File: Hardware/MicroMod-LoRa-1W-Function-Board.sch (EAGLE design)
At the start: 34 parts, among them J11 MICROMOD_STANDARD, Q3 20V/4.2A/52mΩ/1.4W, Q4 600mA/40V, Q5 20V/4.2A/52mΩ/1.4W, Q6 600mA/40V, U1 EEPROM, U4 E19-915M30S

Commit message: Adding panel files
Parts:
- added LOGO2: SPECIAL_INSTRUCTIONS-ORDERING, SparkFun-Aesthetics:SPECIAL_INSTRUCTIONS-ORDERING
- C8: value 68uF -> 47uF; device SparkFun-Capacitors:68UF-POLAR-EIA3528-10V-10%(TANT) -> SparkFun-Capacitors:47UF-POLAR-EIA3528-10V-10%
- J11: device SparkFun-MicroMod-Test:MICROMOD_STANDARD -> SparkFun-MicroMod-Function:MICROMOD_STANDARD
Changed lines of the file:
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@@
 <part name="GND33" library="SparkFun-PowerSymbols" deviceset="GND" device=""/>
 <part name="GND34" library="SparkFun-PowerSymbols" deviceset="GND" device=""/>
-<part name="C8" library="SparkFun-Capacitors" deviceset="68UF-POLAR" device="-EIA3528-10V-10%(TANT)" value="68uF"/>
+<part name="C8" library="SparkFun-Capacitors" deviceset="47UF-POLAR" device="-EIA3528-10V-10%" value="47uF"/>
 <part name="GND2" library="SparkFun-PowerSymbols" deviceset="GND" device=""/>
 <part name="SUPPLY2" library="SparkFun-PowerSymbols" deviceset="VCC" device=""/>
@@
 <part name="E1" library="SparkFun-RF" deviceset="ANTENNA-SMA-GROUNDED" device="EDGE_RPSMA_SMD" value="RP-SMA"/>
 <part name="GND3" library="SparkFun-PowerSymbols" deviceset="GND" device=""/>
-<part name="J11" library="SparkFun-MicroMod-Test" deviceset="MICROMOD" device="_STANDARD"/>
+<part name="J11" library="SparkFun-MicroMod-Function" deviceset="MICROMOD" device="_STANDARD"/>
 <part name="R2" library="SparkFun-Resistors" deviceset="470OHM" device="-0603-1/10W-1%" value="470"/>
 <part name="Q3" library="SparkFun-DiscreteSemi" deviceset="MOSFET_PCH" device="-DMG2305UX-7" value="20V/4.2A/52mΩ/1.4W"/>
@@
 <part name="C4" library="SparkFun-Capacitors" deviceset="0.1UF" device="-0603-25V-(+80/-20%)" value="0.1uF"/>
 <part name="GND10" library="SparkFun-PowerSymbols" deviceset="GND" device=""/>
+<part name="LOGO2" library="SparkFun-Aesthetics" deviceset="SPECIAL_INSTRUCTIONS" device="-ORDERING"/>
 </parts>
 <sheets>
@@
 <attribute name="VALUE" x="5.08" y="17.526" size="1.778" layer="96" align="top-center"/>
 </instance>
+<instance part="LOGO2" gate="G$1" x="226.06" y="22.86" smashed="yes"/>
 </instances>
 <busses>

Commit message: Fix power control circuit. Add example sketch. Add x02 production panels.
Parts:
- removed Q3, Q5: 20V/4.2A/52mΩ/1.4W, SparkFun-DiscreteSemi:MOSFET_PCH-DMG2305UX-7
- removed Q4: 600mA/40V, SparkFun-DiscreteSemi:TRANS_PNP-MMBT4403
- removed R7: 100k, SparkFun-Resistors:100KOHM-0603-1/10W-1%
- added JP1: JUMPER-SMT_2_NO_SILK, SparkFun-Jumpers:JUMPER-SMT_2_NO_SILK
- added Q2: 20V/4.2A/52mΩ/1.4W, SparkFun-DiscreteSemi:MOSFET_PCH-DMG2305UX-7
- added Q8, Q9: 5.8A/30V/35mΩ, SparkFun-DiscreteSemi:MOSFET-NCH-AO3404A
- added R1, R3: 10k, SparkFun-Resistors:10KOHM-0603-1/10W-1%
- Q6: value 600mA/40V -> 20V/4.2A/52mΩ/1.4W; device SparkFun-DiscreteSemi:TRANS_PNP-MMBT4403 -> SparkFun-DiscreteSemi:MOSFET_PCH-DMG2305UX-7
- R4: value 100k -> 10k; device SparkFun-Resistors:100KOHM-0603-1/10W-1% -> SparkFun-Resistors:10KOHM-0603-1/10W-1%
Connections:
- removed net N$11: Q5.G, Q6.C, R7.2
- removed net N$9: Q3.G, Q4.C, R4.2
- new net N$2: Q2.G, Q8.D, R1.1
- new net N$3: Q6.G, Q9.D, R3.1
- new net N$7: JP1.2, R4.1, U1.WP
- net 3.3V: now also Q2.D, R4.2; no longer Q3.D
- net 3.3V_IN: now also Q2.S, R1.2; no longer Q3.S, Q4.E
- net GND: now also JP1.1, Q8.S, Q9.S; no longer R4.1, R7.1, U1.WP
- net PWR_EN: now also Q8.G, Q9.G; no longer Q4.B, Q6.B
- net VCC: now also Q6.D; no longer Q5.D
- net VCC_IN: now also Q6.S, R3.2; no longer Q5.S, Q6.E
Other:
- note added: "VCC: 3.3-5.5V >= 5V Ensures Max Output Power"
- note removed: "0V turns on PNP"
- note removed: "3.3V on gate turns off MOSFET"
- note removed: "VCC: 3.3-5.5V >= 5V Ensures Output Power"
- moved on the sheet: R4

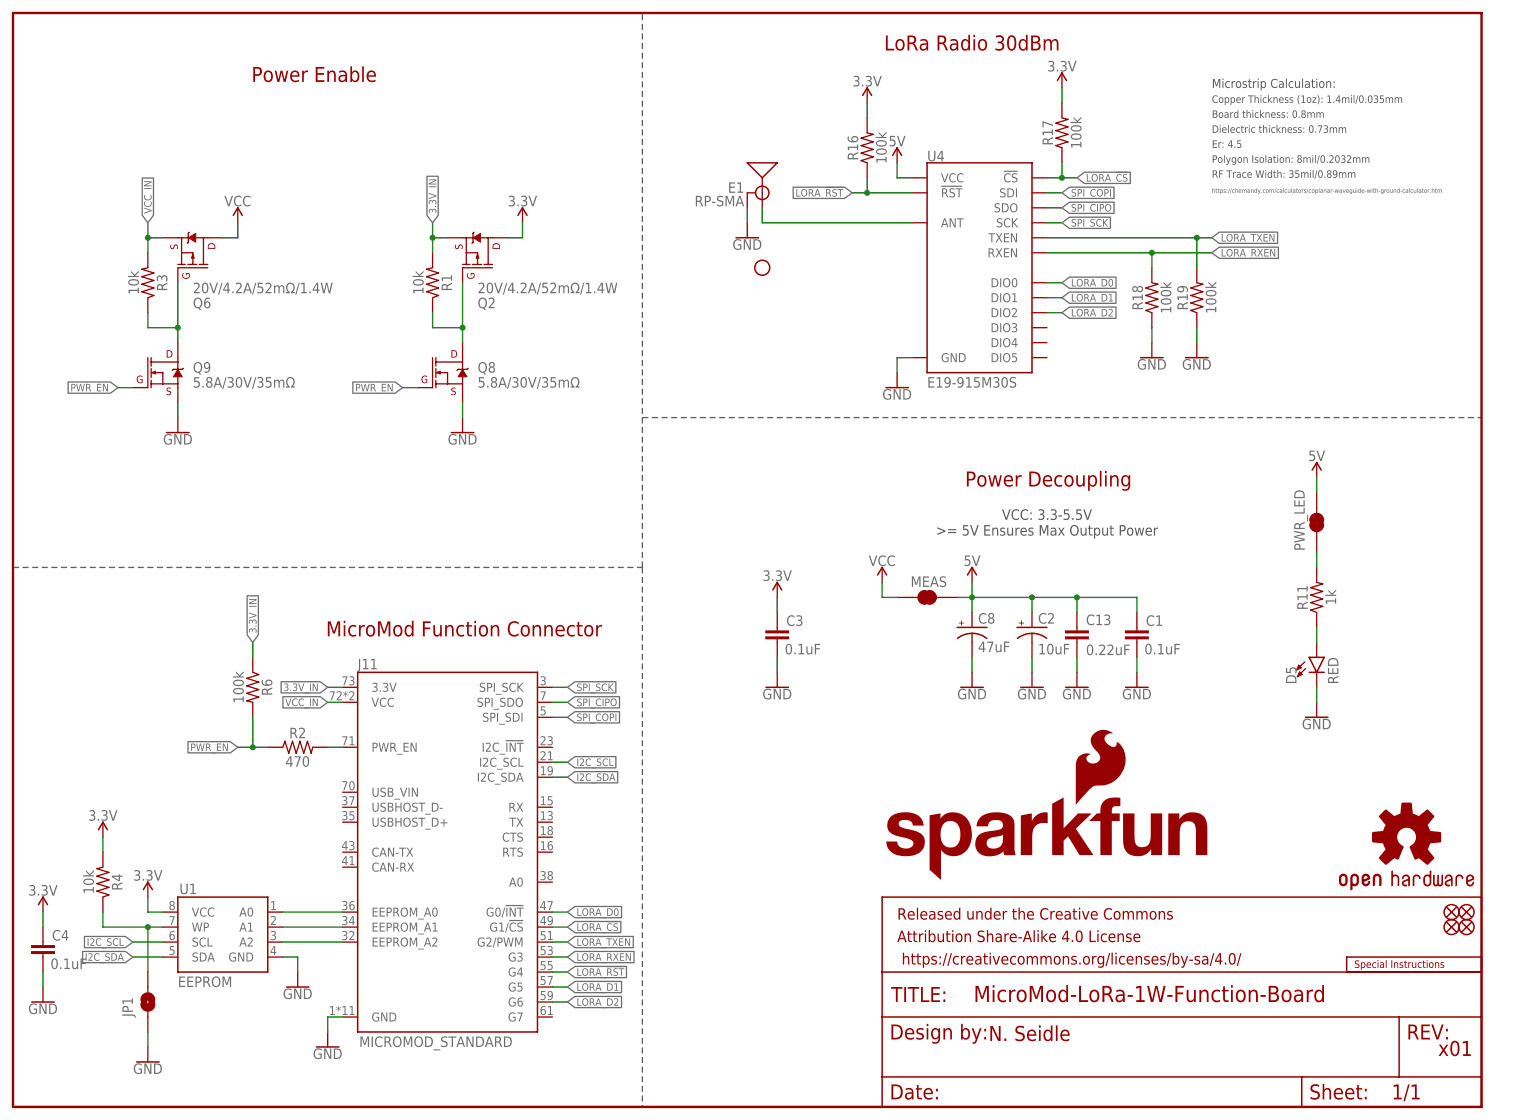
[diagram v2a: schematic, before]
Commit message: Add WP access to card edge.
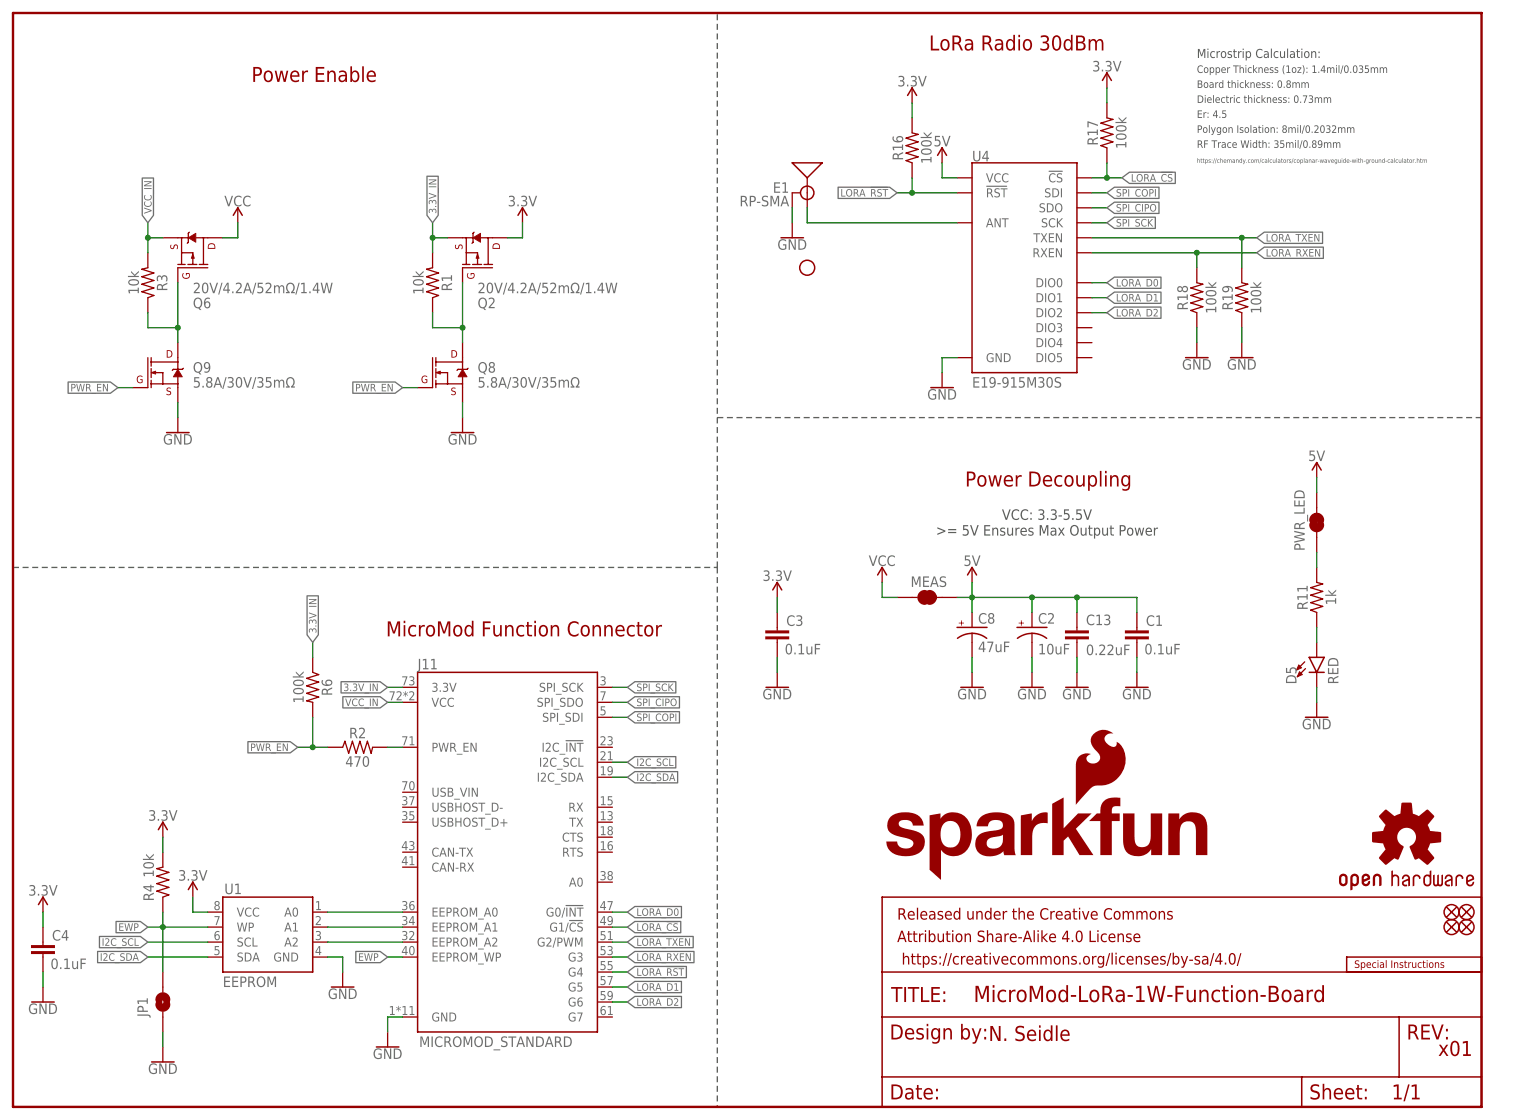
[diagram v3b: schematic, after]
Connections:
- removed net N$7: JP1.2, R4.1, U1.WP
- new net EWP: J11.EEPROM_WP, JP1.2, R4.1, U1.WP
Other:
- moved on the sheet: E1, JP1, R16, R17, R18, R19, R2, R4, R6, U1, U4

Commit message: Update version to v10.
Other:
- note added: "v10"
- note removed: "x01"
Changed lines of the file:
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@@
 &gt;= 5V Ensures Max Output Power</text>
 <text x="165.354" y="11.176" size="2.54" layer="94">N. Seidle</text>
-<text x="241.554" y="8.636" size="2.54" layer="94">x01</text>
+<text x="241.554" y="8.636" size="2.54" layer="94">v10</text>
 <text x="170.18" y="180.34" size="2.54" layer="94" font="vector" align="center">LoRa Radio 30dBm</text>
 <text x="200.66" y="172.72" size="1.27" layer="97">Board thickness: 0.8mm</text>

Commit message: Add SMA center pin. Increase panel gap to facilitate center pin. PCB is still v10.
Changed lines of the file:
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@@
 <part name="C1" library="SparkFun-Capacitors" deviceset="0.1UF" device="-0603-25V-(+80/-20%)" value="0.1uF"/>
 <part name="C2" library="SparkFun-Capacitors" deviceset="10UF-POLAR" device="-EIA3216-16V-10%(TANT)" value="10uF"/>
-<part name="MEAS" library="SparkFun-Jumpers" deviceset="JUMPER-COMBO_2_NC_TRACE" device="" value=""/>
+<part name="MEAS" library="SparkFun-Jumpers" deviceset="JUMPER-COMBO_2_NC_TRACE" device="" value="JUMPER-COMBO_2_NC_TRACE"/>
 <part name="GND6" library="SparkFun-PowerSymbols" deviceset="GND" device=""/>
 <part name="LOGO3" library="SparkFun-Aesthetics" deviceset="OSHW-LOGO" device="MINI"/>
-<part name="PWR_LED" library="SparkFun-Jumpers" deviceset="JUMPER-SMT_2_NC_TRACE" device="_SILK" package3d_urn="urn:adsk.eagle:package:39281/1" value=""/>
+<part name="PWR_LED" library="SparkFun-Jumpers" deviceset="JUMPER-SMT_2_NC_TRACE" device="_SILK" package3d_urn="urn:adsk.eagle:package:39281/1" value="JUMPER-SMT_2_NC_TRACE_SILK"/>
 <part name="R11" library="SparkFun-Resistors" deviceset="1KOHM" device="-0603-1/10W-1%" value="1k"/>
 <part name="D5" library="SparkFun-LED" deviceset="LED-RED" device="0603" value="RED"/>
@@
 <part name="R4" library="SparkFun-Resistors" deviceset="10KOHM" device="-0603-1/10W-1%" value="10k"/>
 <part name="SUPPLY1" library="SparkFun-PowerSymbols" deviceset="3.3V" device=""/>
-<part name="JP1" library="SparkFun-Jumpers" deviceset="JUMPER-SMT_2_NO" device="_SILK" package3d_urn="urn:adsk.eagle:package:39279/1" value=""/>
+<part name="JP1" library="SparkFun-Jumpers" deviceset="JUMPER-SMT_2_NO" device="_SILK" package3d_urn="urn:adsk.eagle:package:39279/1" value="JUMPER-SMT_2_NO_SILK"/>
 </parts>
 <sheets>

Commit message: Updates the design to use the Micromod-function device in the official SFE Eagle Libs
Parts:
- J11: value MICROMOD_STANDARD -> MICROMOD_FUNCTION_STANDARD; device SparkFun-MicroMod-Function:MICROMOD_STANDARD -> SparkFun-MicroMod:MICROMOD_FUNCTION_STANDARD
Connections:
- net LORA_!CS!: now also J11.F1/!CS!; no longer J11.G1/!CS!
- net LORA_!RST!: now also J11.F4; no longer J11.G4
- net LORA_D0: now also J11.F0/!INT!; no longer J11.G0/!INT!
- net LORA_D1: now also J11.F5; no longer J11.G5
- net LORA_D2: now also J11.F6; no longer J11.G6
- net LORA_RXEN: now also J11.F3; no longer J11.G3
- net LORA_TXEN: now also J11.F2/PWM; no longer J11.G2/PWM
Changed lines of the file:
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@@
 <?xml version="1.0" encoding="utf-8"?>
 <!DOCTYPE eagle SYSTEM "eagle.dtd">
-<eagle version="9.6.2">
+<eagle version="9.5.2">
 <drawing>
 <settings>
-<setting alwaysvectorfont="yes"/>
+<setting alwaysvectorfont="no"/>
 <setting verticaltext="up"/>
 </settings>
@@
 <part name="E1" library="SparkFun-RF" deviceset="ANTENNA-SMA-GROUNDED" device="EDGE_RPSMA_SMD" value="RP-SMA"/>
 <part name="GND3" library="SparkFun-PowerSymbols" deviceset="GND" device=""/>
-<part name="J11" library="SparkFun-MicroMod-Function" deviceset="MICROMOD" device="_STANDARD"/>
+<part name="J11" library="SparkFun-MicroMod" deviceset="MICROMOD_FUNCTION" device="_STANDARD"/>
 <part name="R2" library="SparkFun-Resistors" deviceset="470OHM" device="-0603-1/10W-1%" value="470"/>
 <part name="R6" library="SparkFun-Resistors" deviceset="100KOHM" device="-0603-1/10W-1%" value="100k"/>
@@
 <label x="104.14" y="30.48" size="1.27" layer="95" xref="yes"/>
 <wire x1="101.6" y1="30.48" x2="104.14" y2="30.48" width="0.1524" layer="91"/>
-<pinref part="J11" gate="J1" pin="G1/!CS!"/>
+<pinref part="J11" gate="J1" pin="F1/!CS!"/>
 </segment>
 </net>
@@
 <label x="104.14" y="27.94" size="1.27" layer="95" xref="yes"/>
 <wire x1="101.6" y1="27.94" x2="104.14" y2="27.94" width="0.1524" layer="91"/>
-<pinref part="J11" gate="J1" pin="G2/PWM"/>
+<pinref part="J11" gate="J1" pin="F2/PWM"/>
 </segment>
 </net>
@@
 <label x="104.14" y="25.4" size="1.27" layer="95" xref="yes"/>
 <wire x1="101.6" y1="25.4" x2="104.14" y2="25.4" width="0.1524" layer="91"/>
-<pinref part="J11" gate="J1" pin="G3"/>
+<pinref part="J11" gate="J1" pin="F3"/>
 </segment>
 </net>
@@
 <wire x1="101.6" y1="33.02" x2="104.14" y2="33.02" width="0.1524" layer="91"/>
 <label x="104.14" y="33.02" size="1.27" layer="95" xref="yes"/>
-<pinref part="J11" gate="J1" pin="G0/!INT!"/>
+<pinref part="J11" gate="J1" pin="F0/!INT!"/>
 </segment>
 </net>
@@
 <wire x1="101.6" y1="20.32" x2="104.14" y2="20.32" width="0.1524" layer="91"/>
 <label x="104.14" y="20.32" size="1.27" layer="95" xref="yes"/>
-<pinref part="J11" gate="J1" pin="G5"/>
+<pinref part="J11" gate="J1" pin="F5"/>
 </segment>
 </net>
@@
 <wire x1="101.6" y1="17.78" x2="104.14" y2="17.78" width="0.1524" layer="91"/>
 <label x="104.14" y="17.78" size="1.27" layer="95" xref="yes"/>
-<pinref part="J11" gate="J1" pin="G6"/>
+<pinref part="J11" gate="J1" pin="F6"/>
 </segment>
 </net>
@@
 <wire x1="101.6" y1="22.86" x2="104.14" y2="22.86" width="0.1524" layer="91"/>
 <label x="104.14" y="22.86" size="1.27" layer="95" xref="yes"/>
-<pinref part="J11" gate="J1" pin="G4"/>
-</segment>
-</net>
+<pinref part="J11" gate="J1" pin="F4"/>
+</segment>
+</net>
